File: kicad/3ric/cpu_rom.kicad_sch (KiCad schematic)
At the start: 14 parts

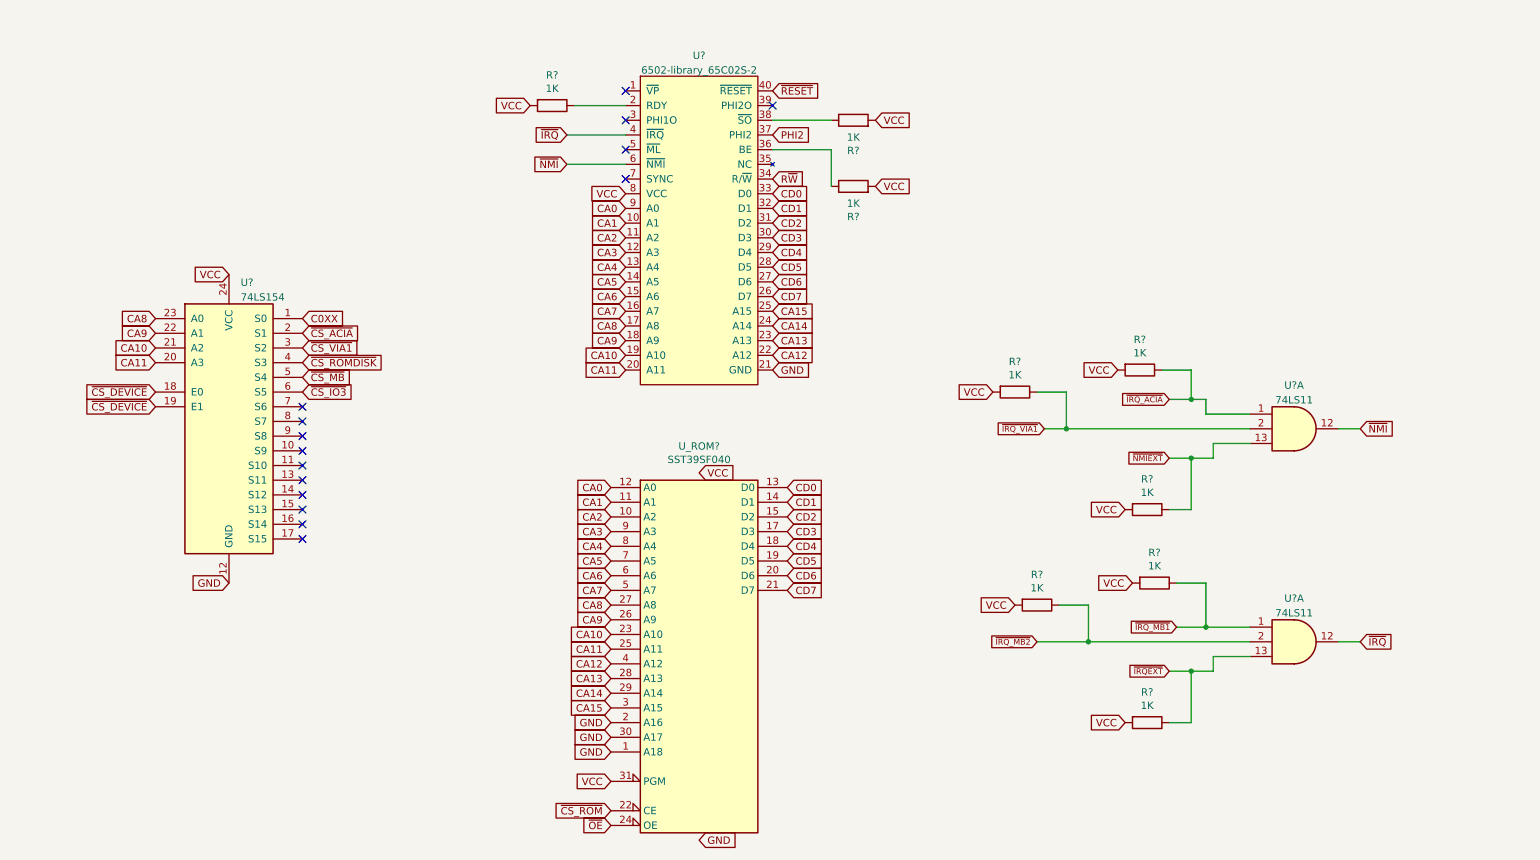
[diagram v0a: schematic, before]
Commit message: upgraded to kicad 8, updates to schematic - added snes controllers, mouse port, many fixes
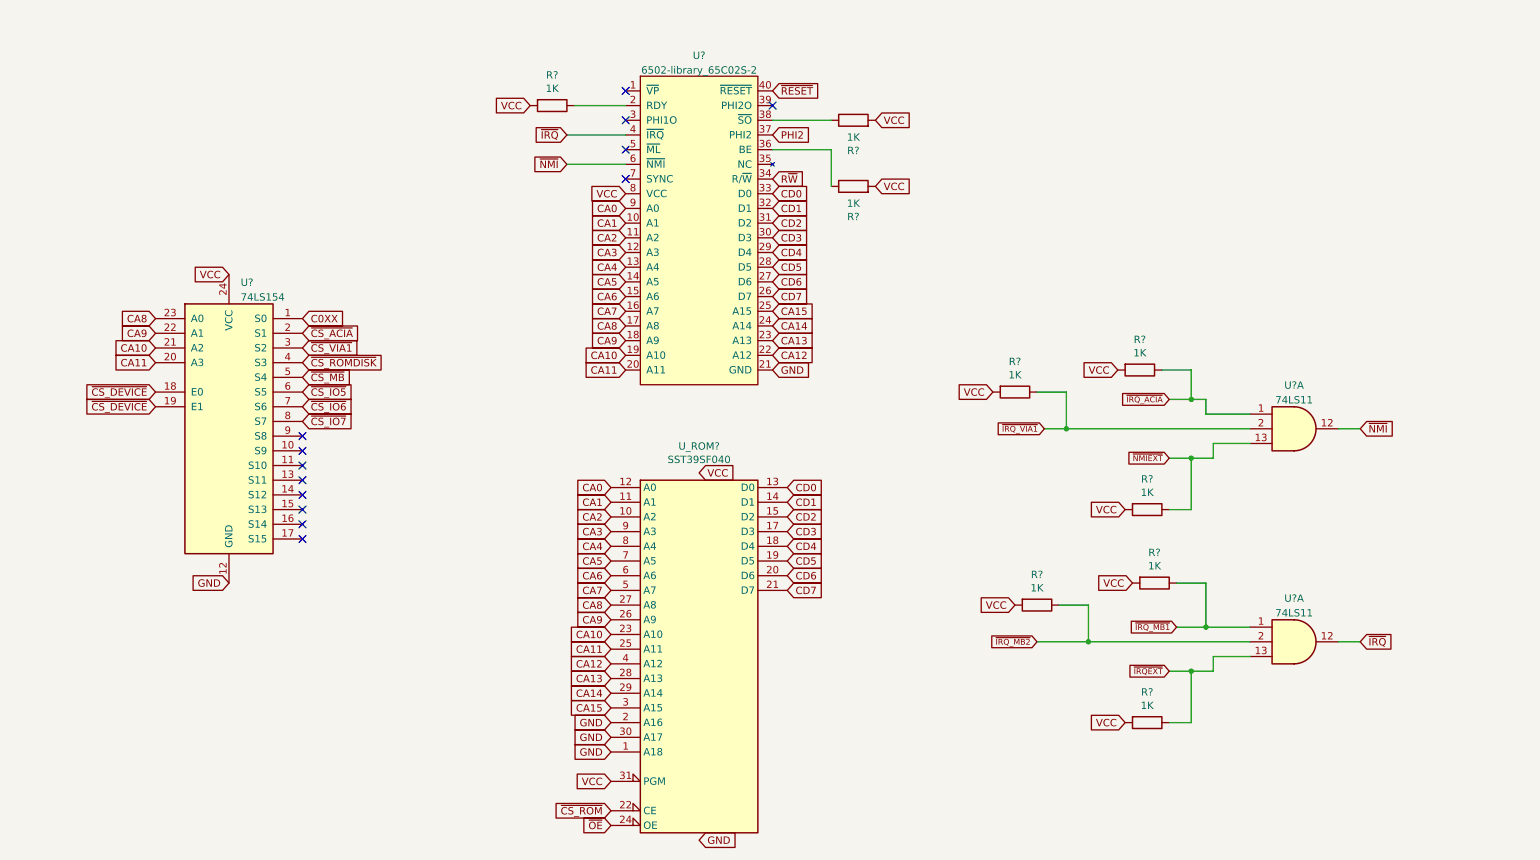
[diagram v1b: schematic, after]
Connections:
- net ~{CS_IO6}: now reaches U?.7 (S6)
- net ~{CS_IO7}: now reaches U?.8 (S7)
- net ~{CS_IO3} renamed ~{CS_IO5}
- no-connect marks 15 -> 13

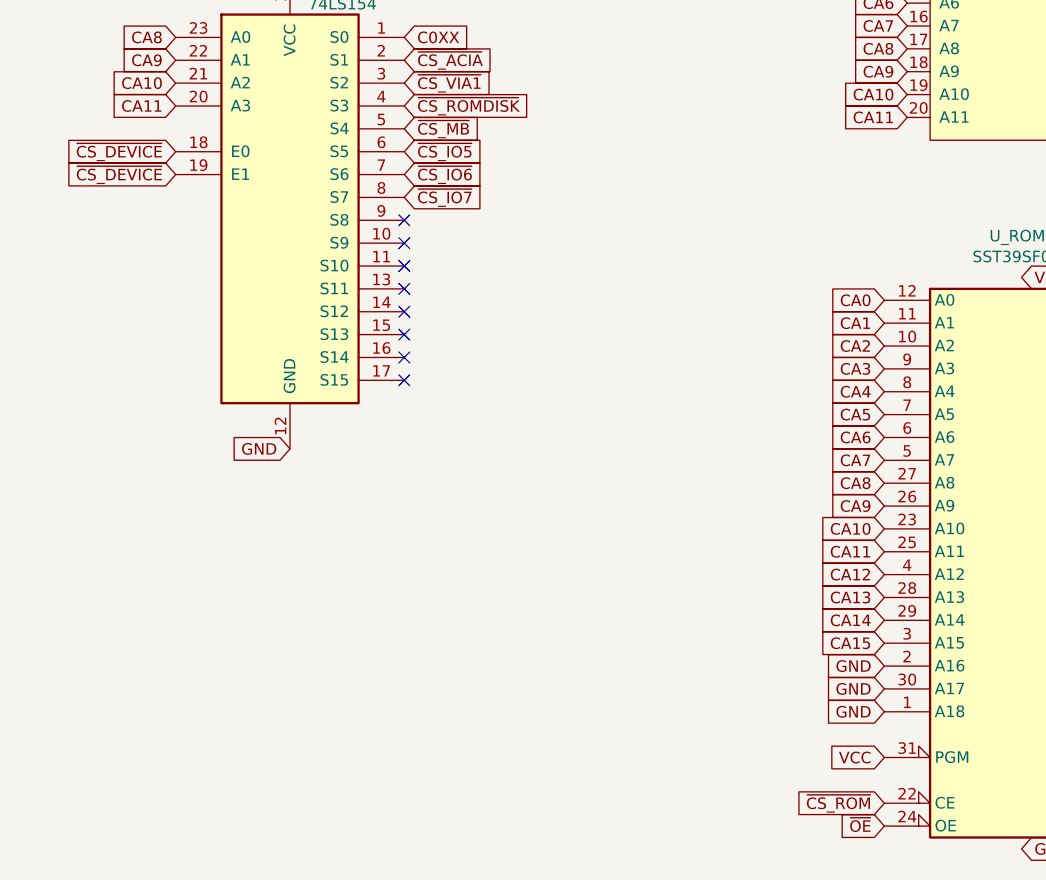
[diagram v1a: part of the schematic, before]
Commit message: update schematic to include disk components
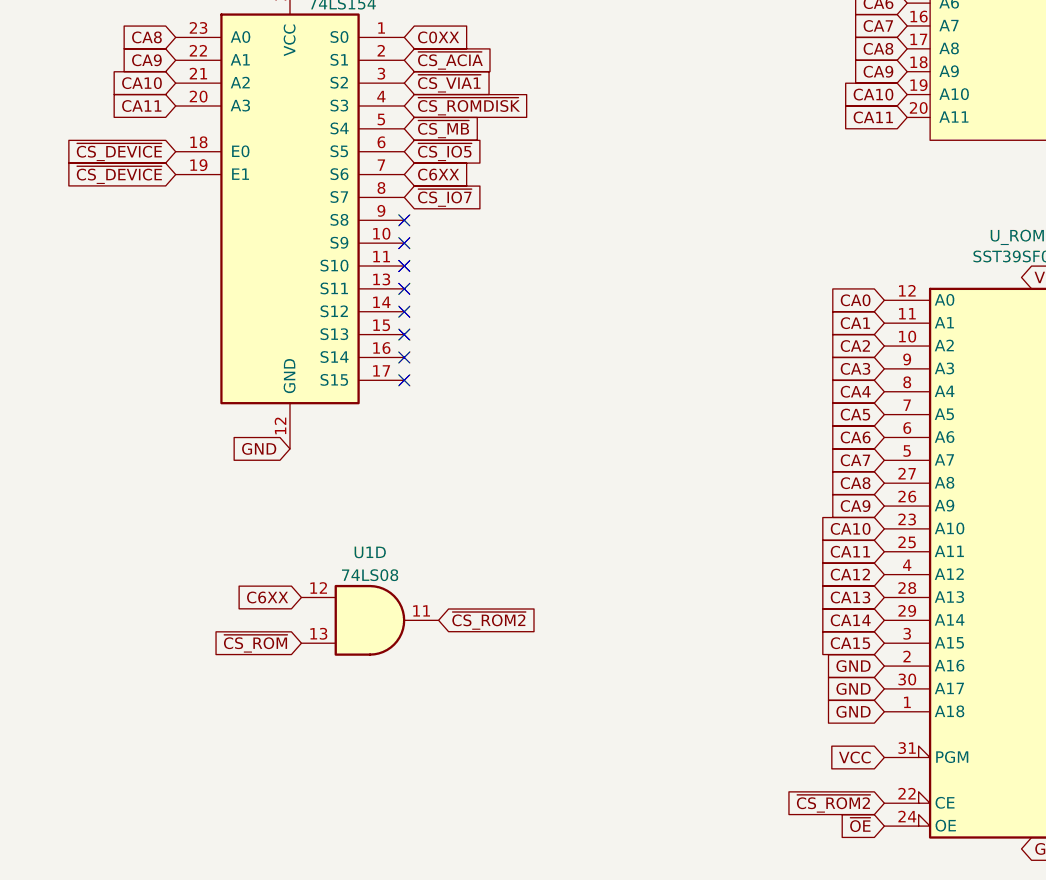
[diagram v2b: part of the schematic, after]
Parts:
- added U1: 74LS08, symbol 74xx:74LS08
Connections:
- net ~{CS_ROM}: now also U1.13; no longer U_ROM?.22 (CE)
- net ~{CS_IO6} renamed C6XX
- net C6XX: now also U1.12
- new net ~{CS_ROM2}: U1.11, U_ROM?.22 (CE)

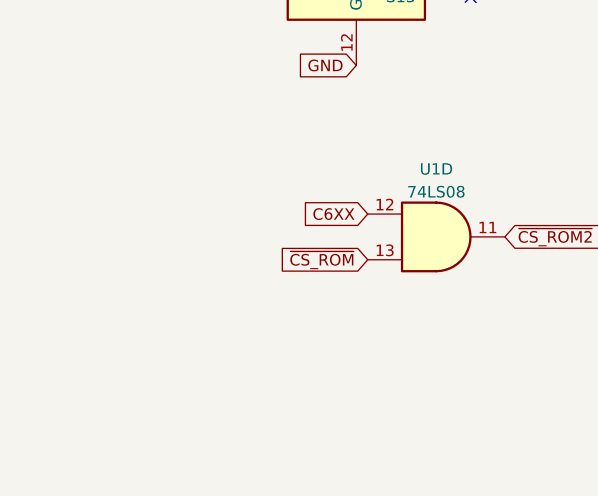
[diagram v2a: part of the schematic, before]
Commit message: update the breadboard map and the schematics
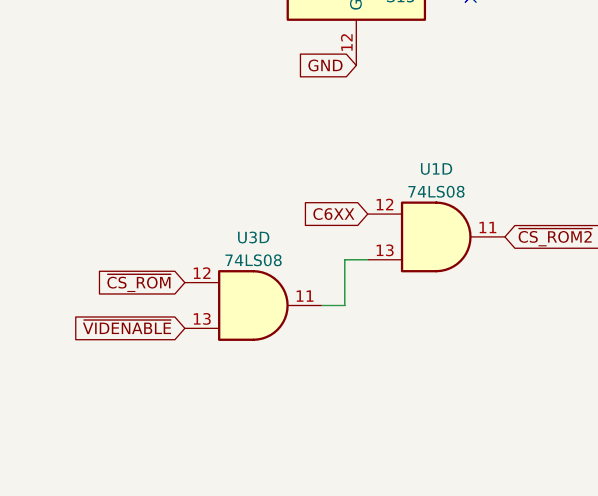
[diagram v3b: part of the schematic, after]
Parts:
- added U3: 74LS08, symbol 74xx:74LS08
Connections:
- net ~{CS_ROM}: now also U3.12; no longer U1.13
- new net: U1.13, U3.11
- new net ~{VIDENABLE}: U3.13
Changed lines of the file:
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@@
+	(wire
+		(pts
+			(xy 54.61 153.67) (xy 54.61 148.59)
+		)
+		(stroke
+			(width 0)
+			(type default)
+		)
+	)
 	(wire
 		(pts
@@
 	(wire
 		(pts
-			(xy 196.85 100.33) (xy 200.66 100.33)
+			(xy 52.07 153.67) (xy 54.61 153.67)
 		)
 		(stroke
@@
 	(wire
 		(pts
-			(xy 200.66 100.33) (xy 232.41 100.33)
+			(xy 196.85 100.33) (xy 200.66 100.33)
 		)
 		(stroke
@@
 	(wire
 		(pts
-			(xy 222.25 105.41) (xy 226.06 105.41)
+			(xy 200.66 100.33) (xy 232.41 100.33)
 		)
 		(stroke
@@
 	(wire
 		(pts
-			(xy 195.58 137.16) (xy 204.47 137.16)
+			(xy 222.25 105.41) (xy 226.06 105.41)
 		)
 		(stroke
@@
 	(wire
 		(pts
-			(xy 224.79 95.25) (xy 224.79 97.79)
+			(xy 195.58 137.16) (xy 204.47 137.16)
 		)
 		(stroke
@@
 	(wire
 		(pts
-			(xy 160.02 52.07) (xy 160.02 58.42)
+			(xy 224.79 95.25) (xy 224.79 97.79)
 		)
 		(stroke
@@
 	(wire
 		(pts
-			(xy 219.71 134.62) (xy 224.79 134.62)
+			(xy 160.02 52.07) (xy 160.02 58.42)
 		)
 		(stroke
@@
 	(wire
 		(pts
-			(xy 204.47 130.81) (xy 199.39 130.81)
+			(xy 219.71 134.62) (xy 224.79 134.62)
 		)
 		(stroke
@@
 	(wire
 		(pts
-			(xy 114.3 49.53) (xy 124.46 49.53)
+			(xy 204.47 130.81) (xy 199.39 130.81)
 		)
 		(stroke
@@
 	(wire
 		(pts
-			(xy 222.25 95.25) (xy 222.25 90.17)
+			(xy 114.3 49.53) (xy 124.46 49.53)
 		)
 		(stroke
@@
 	(wire
 		(pts
-			(xy 226.06 102.87) (xy 232.41 102.87)
+			(xy 222.25 95.25) (xy 222.25 90.17)
 		)
 		(stroke
@@
 	(wire
 		(pts
-			(xy 222.25 151.13) (xy 222.25 142.24)
+			(xy 226.06 102.87) (xy 232.41 102.87)
 		)
 		(stroke
@@
 	(wire
 		(pts
-			(xy 218.44 95.25) (xy 222.25 95.25)
+			(xy 222.25 151.13) (xy 222.25 142.24)
 		)
 		(stroke
@@
 	(wire
 		(pts
-			(xy 114.3 54.61) (xy 124.46 54.61)
+			(xy 218.44 95.25) (xy 222.25 95.25)
 		)
 		(stroke
@@
 	(wire
 		(pts
-			(xy 222.25 90.17) (xy 217.17 90.17)
+			(xy 114.3 54.61) (xy 124.46 54.61)
 		)
 		(stroke
@@
 	(wire
 		(pts
-			(xy 218.44 105.41) (xy 222.25 105.41)
+			(xy 222.25 90.17) (xy 217.17 90.17)
 		)
 		(stroke
@@
 	(wire
 		(pts
-			(xy 251.46 100.33) (xy 247.65 100.33)
+			(xy 218.44 105.41) (xy 222.25 105.41)
 		)
 		(stroke
@@
 	(wire
 		(pts
-			(xy 115.57 44.45) (xy 124.46 44.45)
+			(xy 251.46 100.33) (xy 247.65 100.33)
 		)
 		(stroke
@@
 		)
 	)
+	(wire
+		(pts
+			(xy 54.61 148.59) (xy 57.15 148.59)
+		)
+		(stroke
+			(width 0)
+			(type default)
+		)
+	)
+	(wire
+		(pts
+			(xy 115.57 44.45) (xy 124.46 44.45)
+		)
+		(stroke
+			(width 0)
+			(type default)
+		)
+	)
 	(global_label "~{CS_MB}"
 		(shape input)
@@
 		)
 	)
+	(global_label "~{VIDENABLE}"
+		(shape input)
+		(at 36.83 156.21 180)
+		(fields_autoplaced yes)
+		(effects
+			(font
+				(size 1.27 1.27)
+			)
+			(justify right)
+		)
+		(property "Intersheetrefs" "${INTERSHEET_REFS}"
+			(at 23.8662 156.21 0)
+			(effects
+				(font
+					(size 1.27 1.27)
+				)
+				(justify right)
+				(hide yes)
+			)
+		)
+	)
 	(global_label "~{NMI}"
 		(shape input)
@@
 		)
 	)
+	(global_label "~{CS_ROM}"
+		(shape input)
+		(at 36.83 151.13 180)
+		(fields_autoplaced yes)
+		(effects
+			(font
+				(size 1.27 1.27)
+			)
+			(justify right)
+		)
+		(property "Intersheetrefs" "${INTERSHEET_REFS}"
+			(at -113.03 240.03 0)
+			(effects
+				(font
+					(size 1.27 1.27)
+				)
+				(justify left)
+				(hide yes)
+			)
+		)
+	)
 	(global_label "CA3"
 		(shape input)
@@
 					(size 1.27 1.27)
 				)
-				(hide yes)
-			)
-		)
-	)
-	(global_label "~{CS_ROM}"
-		(shape input)
-		(at 57.15 148.59 180)
-		(fields_autoplaced yes)
-		(effects
-			(font
-				(size 1.27 1.27)
-			)
-			(justify right)
-		)
-		(property "Intersheetrefs" "${INTERSHEET_REFS}"
-			(at -92.71 237.49 0)
-			(effects
-				(font
-					(size 1.27 1.27)
-				)
-				(justify left)
 				(hide yes)
 			)
@@
 				)
 			)
+		)
+	)
+	(symbol
+		(lib_id "74xx:74LS08")
+		(at 44.45 153.67 0)
+		(unit 4)
+		(exclude_from_sim no)
+		(in_bom yes)
+		(on_board yes)
+		(dnp no)
+		(fields_autoplaced yes)
+		(property "Reference" "U3"
+			(at 44.45 146.1602 0)
+			(effects
+				(font
+					(size 1.27 1.27)
+				)
+			)
+		)
+		(property "Value" "74LS08"
+			(at 44.45 148.6971 0)
+			(effects
+				(font
+					(size 1.27 1.27)
+				)
+			)
+		)
+		(property "Footprint" ""
+			(at 44.45 153.67 0)
+			(effects
+				(font
+					(size 1.27 1.27)
+				)
+				(hide yes)
+			)
+		)
+		(property "Datasheet" "http://www.ti.com/lit/gpn/sn74LS08"
+			(at 44.45 153.67 0)
+			(effects
+				(font
+					(size 1.27 1.27)
+				)
+				(hide yes)
+			)
+		)
+		(property "Description" ""
+			(at 44.45 153.67 0)
+			(effects
+				(font
+					(size 1.27 1.27)
+				)
+				(hide yes)
+			)
+		)
+		(pin "1"
+		)
+		(pin "2"
+		)
+		(pin "3"
+		)
+		(pin "4"
+		)
+		(pin "5"
+		)
+		(pin "6"
+		)
+		(pin "10"
+		)
+		(pin "8"
+		)
+		(pin "9"
+		)
+		(pin "11"
+		)
+		(pin "12"
+		)
+		(pin "13"
+		)
+		(pin "14"
+		)
+		(pin "7"
+		)
+		(instances
+			(project "3ric"
+				(path "/e63e39d7-6ac0-4ffd-8aa3-1841a4541b55/8b246c3b-322e-4fcf-a8df-6ee4f32565fa"
+					(reference "U3")
+					(unit 4)
+				)
+			)

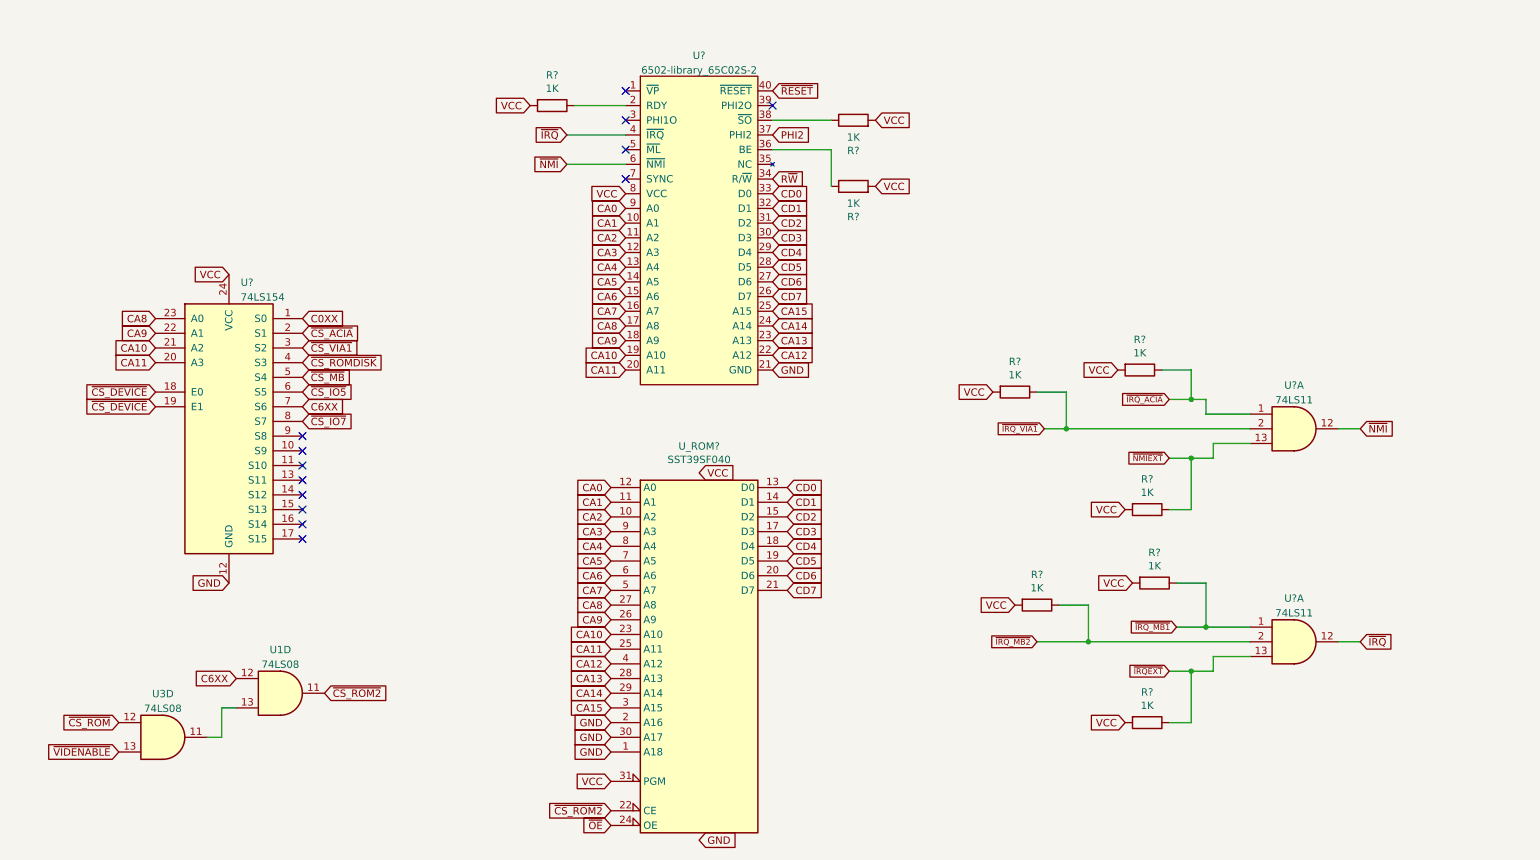
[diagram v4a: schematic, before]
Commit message: update schematic based on breadboard
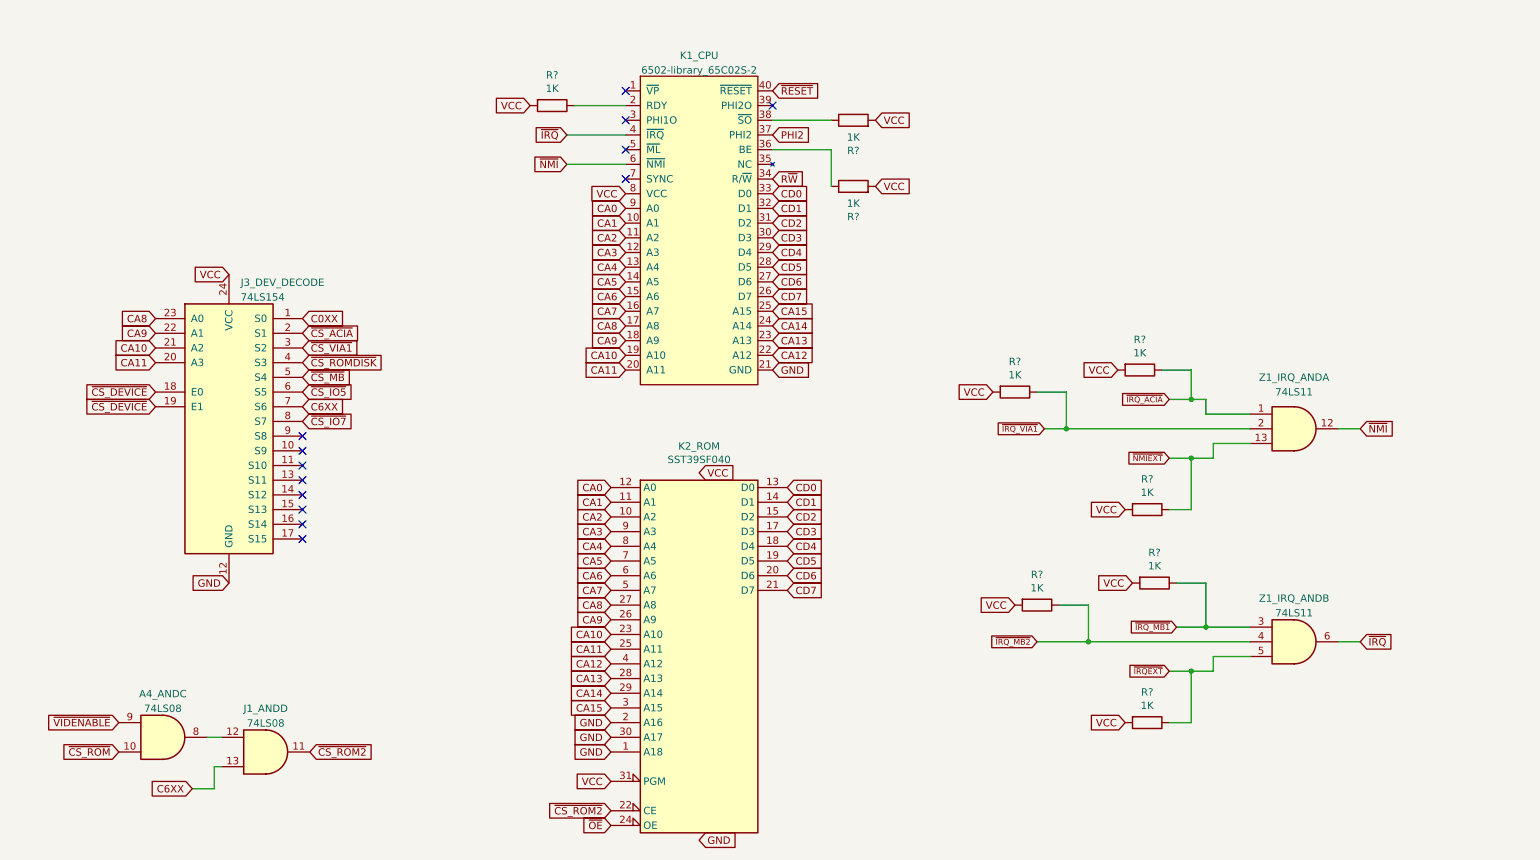
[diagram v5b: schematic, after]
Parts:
- removed U1: 74LS08, symbol 74xx:74LS08
- added J1_AND: 74LS08, symbol 74xx:74LS08
- gave numbers to parts that had none: 4
- renumbered U3 to A4_AND
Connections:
- net C6XX: now also J1_AND.13
- net ~{CS_ROM2}: now also J1_AND.11
- net ~{CS_ROM}: now also A4_AND.10; no longer A4_AND.12
- net ~{IRQEXT}: now also Z1_IRQ_AND.5; no longer Z1_IRQ_AND.13
- net ~{IRQ_MB1}: now also Z1_IRQ_AND.3; no longer Z1_IRQ_AND.1
- net ~{IRQ_MB2}: now also Z1_IRQ_AND.4; no longer Z1_IRQ_AND.2
- net ~{IRQ}: now also Z1_IRQ_AND.6; no longer Z1_IRQ_AND.12
- net ~{VIDENABLE}: now also A4_AND.9; no longer A4_AND.13
- new net: A4_AND.8, J1_AND.12
